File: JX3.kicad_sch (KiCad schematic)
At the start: 1 part

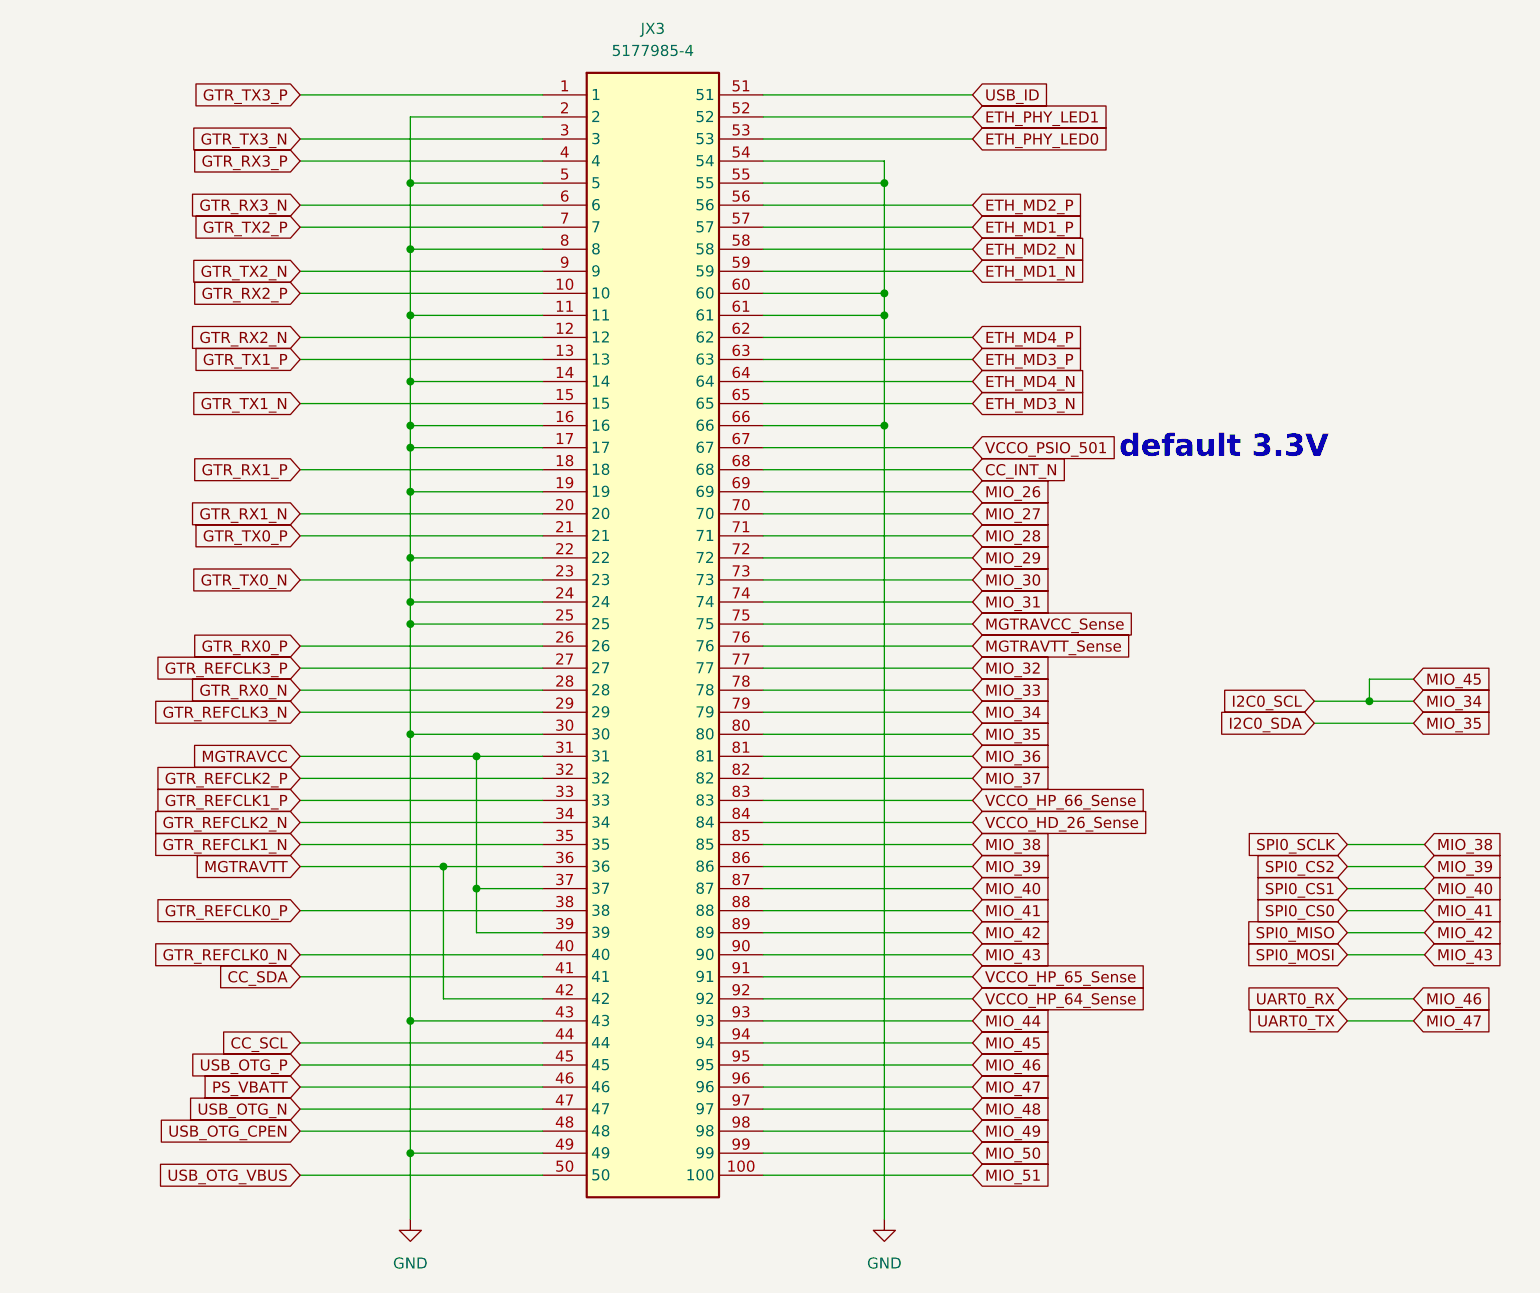
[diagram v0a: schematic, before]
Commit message: moved jtag connector, added holes for all power supplies, fixed most of DRC
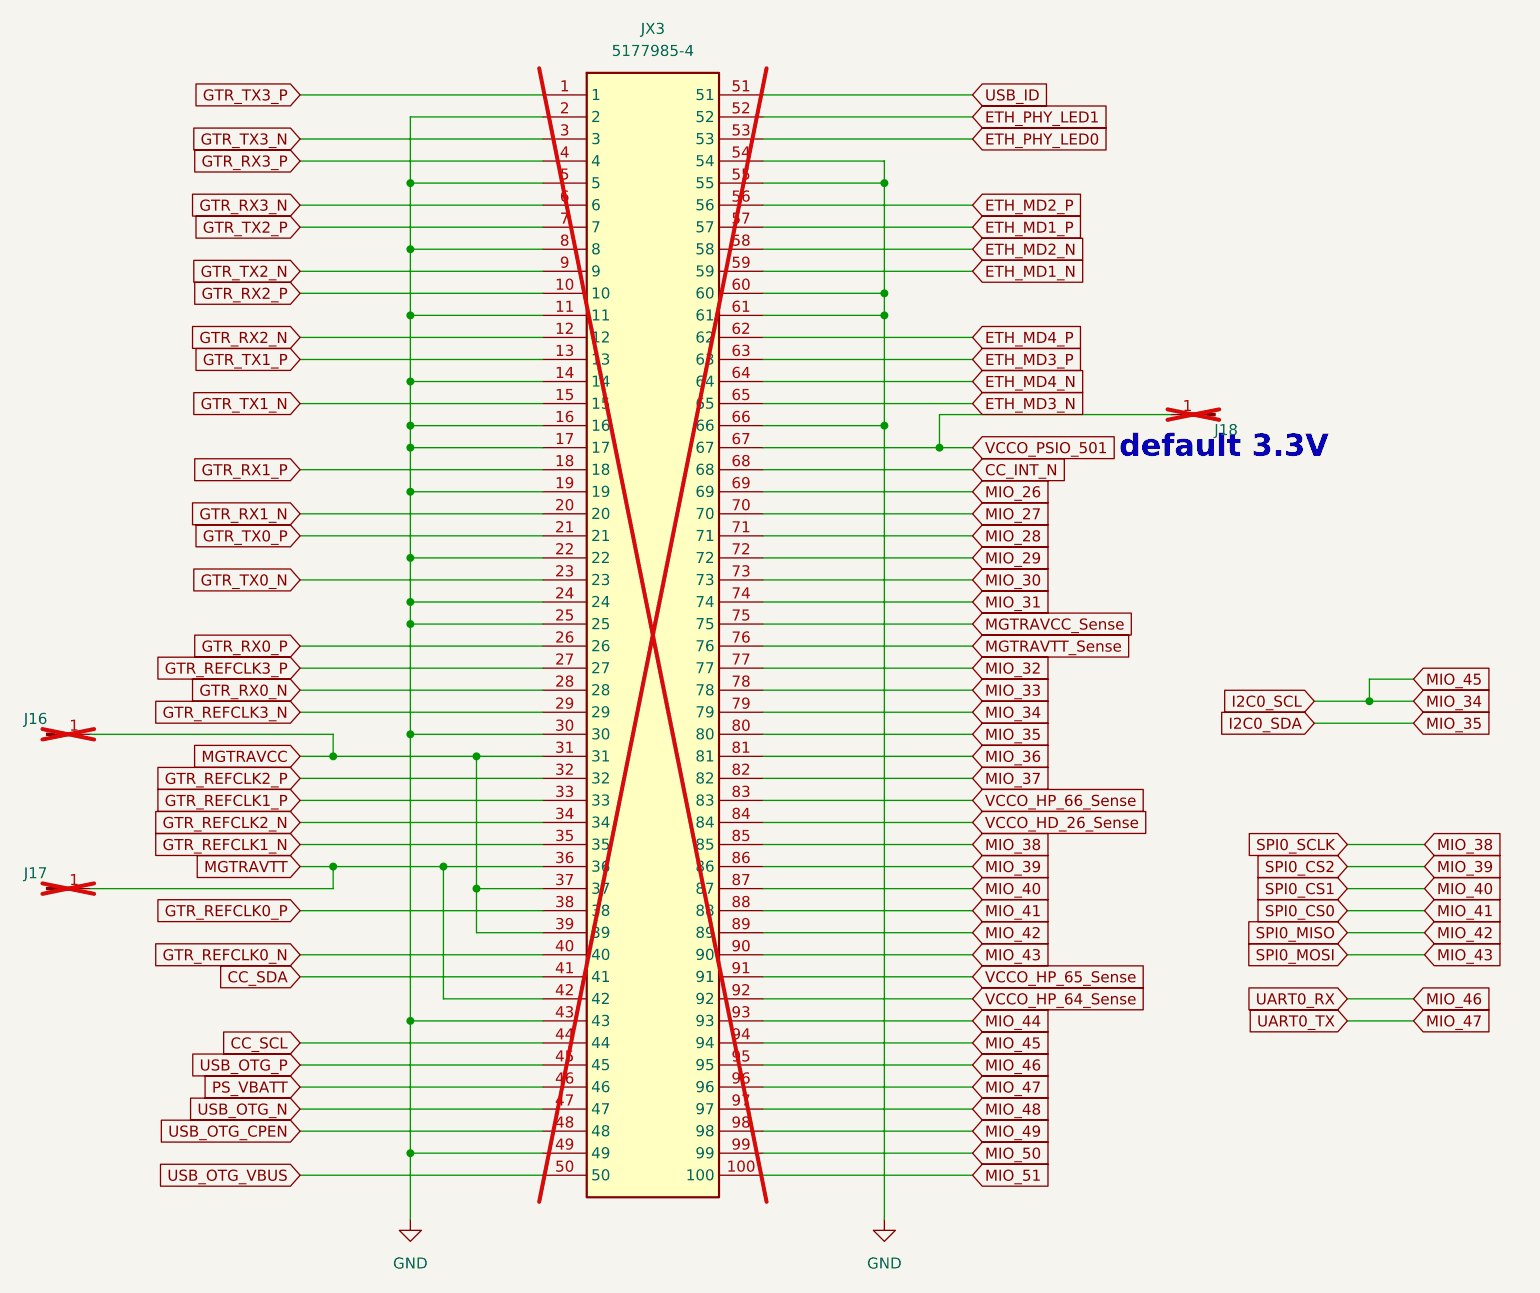
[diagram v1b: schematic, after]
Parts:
- added J16, J17, J18: Conn_01x01_Pin, Connector_PinHeader_2.00mm:PinHeader_1x01_P2.00mm_Horizontal, symbol Connector:Conn_01x01_Pin
- JX3: now not fitted
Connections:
- net MGTRAVCC: now also J16.1 (Pin_1)
- net MGTRAVTT: now also J17.1 (Pin_1)
- net VCCO_PSIO_501: now also J18.1 (Pin_1)
